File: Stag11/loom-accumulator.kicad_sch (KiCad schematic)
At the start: 33 parts, among them M1 AIL FAN

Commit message: Added dummy segment loom
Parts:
- removed Conn?: Molex_2x2P_Vertical, symbol Connectors_SUFST:Molex_2x2P_Vertical
- removed Conn? (x5): Molex_2x2P_Horizontal, symbol Connectors_SUFST:Molex_2x2P_Horizontal
- removed Conn? (x3): Deutsch_DTM_4S_Pin, symbol Connectors_SUFST:Deutsch_DTM_4S_Pin
- removed Conn?: AMPHENOL-21P-Pannel, symbol Connectors_SUFST:AMPHENOL-21P-Pannel
- added J3, J4: Conn_01x12, symbol Connector_Generic:Conn_01x12
- added J5, J6, J7: ATM064S, symbol Connector_Generic:Conn_01x04
- added SegmentPower, SegmentPower1: Deutsch_DTM_6P_Pin, symbol Connectors_SUFST:Deutsch_DTM_6P_Pin
- added SegmentSignals, SegmentSignals1: Deutsch_DTM_12P_Pin, symbol Connectors_SUFST:Deutsch_DTM_12P_Pin
- added XK1A: Conn_01x08, symbol Connector_Generic:Conn_01x08
- added XLA+, XLA-: Conn_01x02, symbol Connector_Generic:Conn_01x02
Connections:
- net CAN.CHARGER.LOW is gone; now on net CAN.CHARGER.HIGH: CONN?.20 (Pin_20), R1.1
- net +AIR.AUX.EXC: now also J3.7 (Pin_7), J6.2 (Pin_2); no longer Conn?.28
- net +AIR.AUX.GND: now also J3.8 (Pin_8), J6.1 (Pin_1); no longer Conn?.29
- net +AIR.EXC: now also J3.6 (Pin_6), J6.4 (Pin_4)
- net +AIR.GND: now also J3.1 (Pin_1), J6.3 (Pin_3), J7.3 (Pin_3), SegmentPower.2; no longer Conn?.1, Conn?.2
- net -AIR.AUX.EXC: now also J3.4 (Pin_4), J7.2 (Pin_2); no longer Conn?.26
- net -AIR.AUX.GND: now also J3.5 (Pin_5), J7.1 (Pin_1); no longer Conn?.27
- net -AIR.EXC: now also J3.3 (Pin_3), J7.4 (Pin_4); no longer Conn?.14
- net BMS.EXC: no longer Conn?.4
- net CAN.S.HIGH: no longer Conn?.11, Conn?.9
- net CAN.S.LOW: no longer Conn?.10, Conn?.12
- net CHASSIS.GND: now also XK1A.3 (Pin_3), XK1A.4 (Pin_4); no longer Conn?.15
- net CLOSE_HIGH_AIR_IN: now also SegmentSignals.4; no longer Conn?.19
- net EXC: now also SegmentPower.3
- net IMD.EXC: now also XK1A.2 (Pin_2); no longer Conn?.5, SP?.1
- net IMD.OK: now also XK1A.8 (Pin_8); no longer Conn?.16
- net INV.CLOSE.PCHG: now also J4.5 (Pin_5), SegmentSignals.1; no longer Conn?.20
- net ISOLATOR.EXC: no longer Conn?.3, R2.1, SP?.1
- net PCHG.AUX.EXC: now also J3.11 (Pin_11), J5.2 (Pin_2); no longer Conn?.24
- net PCHG.AUX.GND: now also J3.12 (Pin_12), J5.1 (Pin_1); no longer Conn?.25
- net PCHG.EXC: now also J3.9 (Pin_9), J5.4 (Pin_4)
- net PCHG.GND: now also J3.10 (Pin_10), J5.3 (Pin_3)
- net SHUT.TRC.IN: now also J3.2 (Pin_2)
- net TS.ON: now also J4.2 (Pin_2); no longer Conn?.18
- net TSAC.HVS.EXC: now also J4.11 (Pin_11), SegmentPower.4; no longer Conn?.6
- net TSAC.HVS.GND: now also J4.10 (Pin_10), SegmentPower.5; no longer Conn?.7
- net ~{BMS.DISCHARGE.ENABLE}: no longer Conn?.30
- net ~{BMS.FAULT}: no longer Conn?.31
- net ~{TS.DETECTED}: now also J4.9 (Pin_9); no longer Conn?.8
- net +AIR.INTENDED.ON: no longer names the net of Conn?.21
- net -AIR.INTENDED.ON: no longer names the net of Conn?.22
- net PCHG.INTENDED.ON: no longer names the net of Conn?.23
- net SHUT.IN: no longer names the net of Conn?.13
- net TS.READY: no longer names the net of Conn?.17
- new net: J4.12 (Pin_12), SegmentSignals.6
- new net IMD.EXC_SPLICE: SP?.1
- new net IMD.GND: XK1A.1 (Pin_1)
- new net ISOLATOR.EXC_SPLICE: R2.1, SP?.1
- new net PCHG.CLOSE.+AIR: J4.4 (Pin_4), SegmentSignals.2
- new net SEGMENT.SHUT.IN: J4.1 (Pin_1), SegmentPower.1
- new net ~{CHARGE.ENABLE.INTERLOCKED}: J4.3 (Pin_3), SegmentSignals.3
- no-connect marks 81 -> 50
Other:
- note added: "IMD"
- note removed: "Add 'devices' to show how ATM conns work for the relays"
- note removed: "BATT+"
- note removed: "BATT-"
- note removed: "DC LINK"
- note removed: "RING TERMINAL ON AIR"
- note removed: "Ring terminal on bolt"
- note removed: "Splice in contact"
- moved on the sheet: CONN?, Conn?, J?, M1, SP?

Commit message: Mostly finished new accumulator loom
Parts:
- removed Conn? (x2): Molex_2x1P_Horizontal_THT, symbol Connectors_SUFST:Molex_2x1P_Horizontal_THT
- removed F?: 100A, symbol Device:Fuse
- added A1: ACCUMULATOR, symbol Device:Battery
- added Conn9, DCLINK+: Banana Plug, symbol Connectors_SUFST:Banana Plug
- added DCLINK, SIGNALS: Conn_01x04, symbol Connector_Generic:Conn_01x04
- added F1: 200A, symbol Device:Fuse
- added HV+ (x2), HV- (x2), PWR: Conn_01x02, symbol Connector_Generic:Conn_01x02
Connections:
- net BMS.Charge.EXC is gone; now on net ACCU.EXC: CONN?.3 (Pin_3)
- net BMS.EXC is gone; now on net ACCU.EXC: CONN?.2 (Pin_2)
- net EXC is gone; now on net +AIR.GND: SegmentPower.3
- net IMD.EXC is gone; now on net ACCU.EXC: XK1A.2 (Pin_2)
- net IMD.GND is gone; now on net +AIR.GND: XK1A.1 (Pin_1)
- net ISOLATOR.EXC_SPLICE is gone; now on net ACCU.EXC: R2.1, SP?.1
- net +AIR.GND: now also Conn?.5, SegmentPower1.3, XK1A.4 (Pin_4), PWR.2 (Pin_2); no longer SegmentPower.2
- net AIL.HV+: now also XLA+.2 (Pin_2), DCLINK+.1, DCLINK.1 (Pin_1), HV+.1 (Pin_1); no longer SP?.1
- net AIL.HV-: now also XLA-.2 (Pin_2), Conn9.1, HV-.2 (Pin_2); no longer SP?.1
- net BMS.CHARGER.SAFETY: now also Conn?.37
- net BMS.CUR_SEN.EXC: now also SegmentSignals.12, SegmentSignals1.12
- net BMS.CUR_SEN.GND: now also SegmentSignals.10, SegmentSignals1.10
- net BMS.CUR_SEN.HIGH: now also SegmentSignals.11, SegmentSignals1.11
- net BMS.CUR_SEN.LOW: now also SegmentSignals.9, SegmentSignals1.9
- net CAN.CHARGER.HIGH: now also Conn?.36; no longer CONN?.20 (Pin_20), R1.1
- net CAN.S.HIGH: now also Conn?.14; no longer SP?.1
- net CAN.S.LOW: now also Conn?.15; no longer SP?.1
- net CHASSIS.GND: now also Conn?.6, SegmentPower.6, SegmentPower1.6; no longer XK1A.4 (Pin_4)
- net CLOSE_HIGH_AIR_IN: now also Conn?.8, SegmentSignals.2, SegmentSignals1.2, SIGNALS.3 (Pin_3); no longer SegmentSignals.4
- net CLOSE_HIGH_AIR_OUT: now also J4.4 (Pin_4), SIGNALS.4 (Pin_4)
- net IMD.OK: now also Conn?.11, SegmentSignals.6, SegmentSignals1.6
- net INV.CLOSE.PCHG: now also Conn?.7, SegmentSignals1.1
- net TS.ON: now also Conn?.9, SegmentSignals.4, SegmentSignals1.4
- net TSAC.HVS.EXC: now also Conn?.2, SegmentPower1.4
- net TSAC.HVS.GND: now also Conn?.3, SegmentPower1.5
- net ~{BMS.DISCHARGE.ENABLE}: now also Conn?.16
- net ~{BMS.FAULT}: now also Conn?.12
- net ~{CHARGE.ENABLE.INTERLOCKED}: now also Conn?.38, SegmentSignals1.3
- net ~{TS.DETECTED}: now also J4.12 (Pin_12); no longer J4.9 (Pin_9)
- net SHUT.IN: now reaches SegmentPower1.1
- net SHUT.IN: now also Conn?.1, Conn?.34, SegmentPower.1
- net ACCU.EXC: now reaches SegmentPower1.2
- net ACCU.EXC: now also Conn?.4, SegmentPower.2, PWR.1 (Pin_1)
- net TS.READY: now reaches Conn?.10
- net TS.READY: now also J4.1 (Pin_1), SegmentSignals.5, SegmentSignals1.5
- net TSAL.GREEN.LIGHT: now reaches Conn?.13
- net TSAL.GREEN.LIGHT: now also J4.9 (Pin_9), SegmentSignals.7, SegmentSignals1.7
- net CAN.CHARGER.LOW: now reaches Conn?.35
- net CAN.CHARGER.LOW: now also CONN?.20 (Pin_20), R1.1
- removed net PCHG.CLOSE.+AIR: J4.4 (Pin_4), SegmentSignals.2
- removed net SEGMENT.SHUT.IN: J4.1 (Pin_1), SegmentPower.1
- new net: A1.1 (+), HV+.1 (Pin_1)
- new net: A1.2 (-), F1.2
- new net: F1.1, HV-.2 (Pin_2)
- new net AIR+_SPLICE: SP?.1
- new net AIR-_SPLICE: SP?.1
- new net CAN.S.HIGH_SPLICE: SP?.1
- new net CAN.S.LOW_SPLICE: SP?.1
- no-connect marks 50 -> 56
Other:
- note added: "ACCU TOP"
- note added: "CAR"
- note added: "CHARGER"
- note added: "CURRENT SENSOR"
- note added: "HV"
- note added: "HV CONNECTOR"
- note added: "ISOLATOR BOARD"
- note added: "LV"
- note added: "SEGMENT"
- note removed: "CHECK FUSE VALUE"
- note removed: "Change how HV splices work to be over the isolation line and physically connecting o the airs and precharge etc"
- note removed: "HV CONNECTIONS"
- note removed: "Isolator Board"
- note removed: "NEEDS HV CONNECTOR INTERLOCK ADDED"
- moved on the sheet: CONN?, Conn?, J?, M1, XK1A, XLA+, XLA-

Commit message: updates
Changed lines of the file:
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@@
 	)
 	(junction
-		(at 154.94 205.74)
-		(diameter 0)
-		(color 0 0 0 0)
-	)
-	(junction
 		(at 138.43 318.77)
 		(diameter 0)
@@
 	(wire
 		(pts
-			(xy 154.94 203.2) (xy 154.94 205.74)
-		)
-		(stroke
-			(width 0)
-			(type default)
-		)
-	)
-	(wire
-		(pts
 			(xy 68.58 88.9) (xy 125.73 88.9)
 		)
@@
 	)
 	(label "INV.CLOSE.+AIR"
-		(at 154.94 203.2 270)
+		(at 154.94 205.74 270)
 		(fields_autoplaced yes)
 		(effects

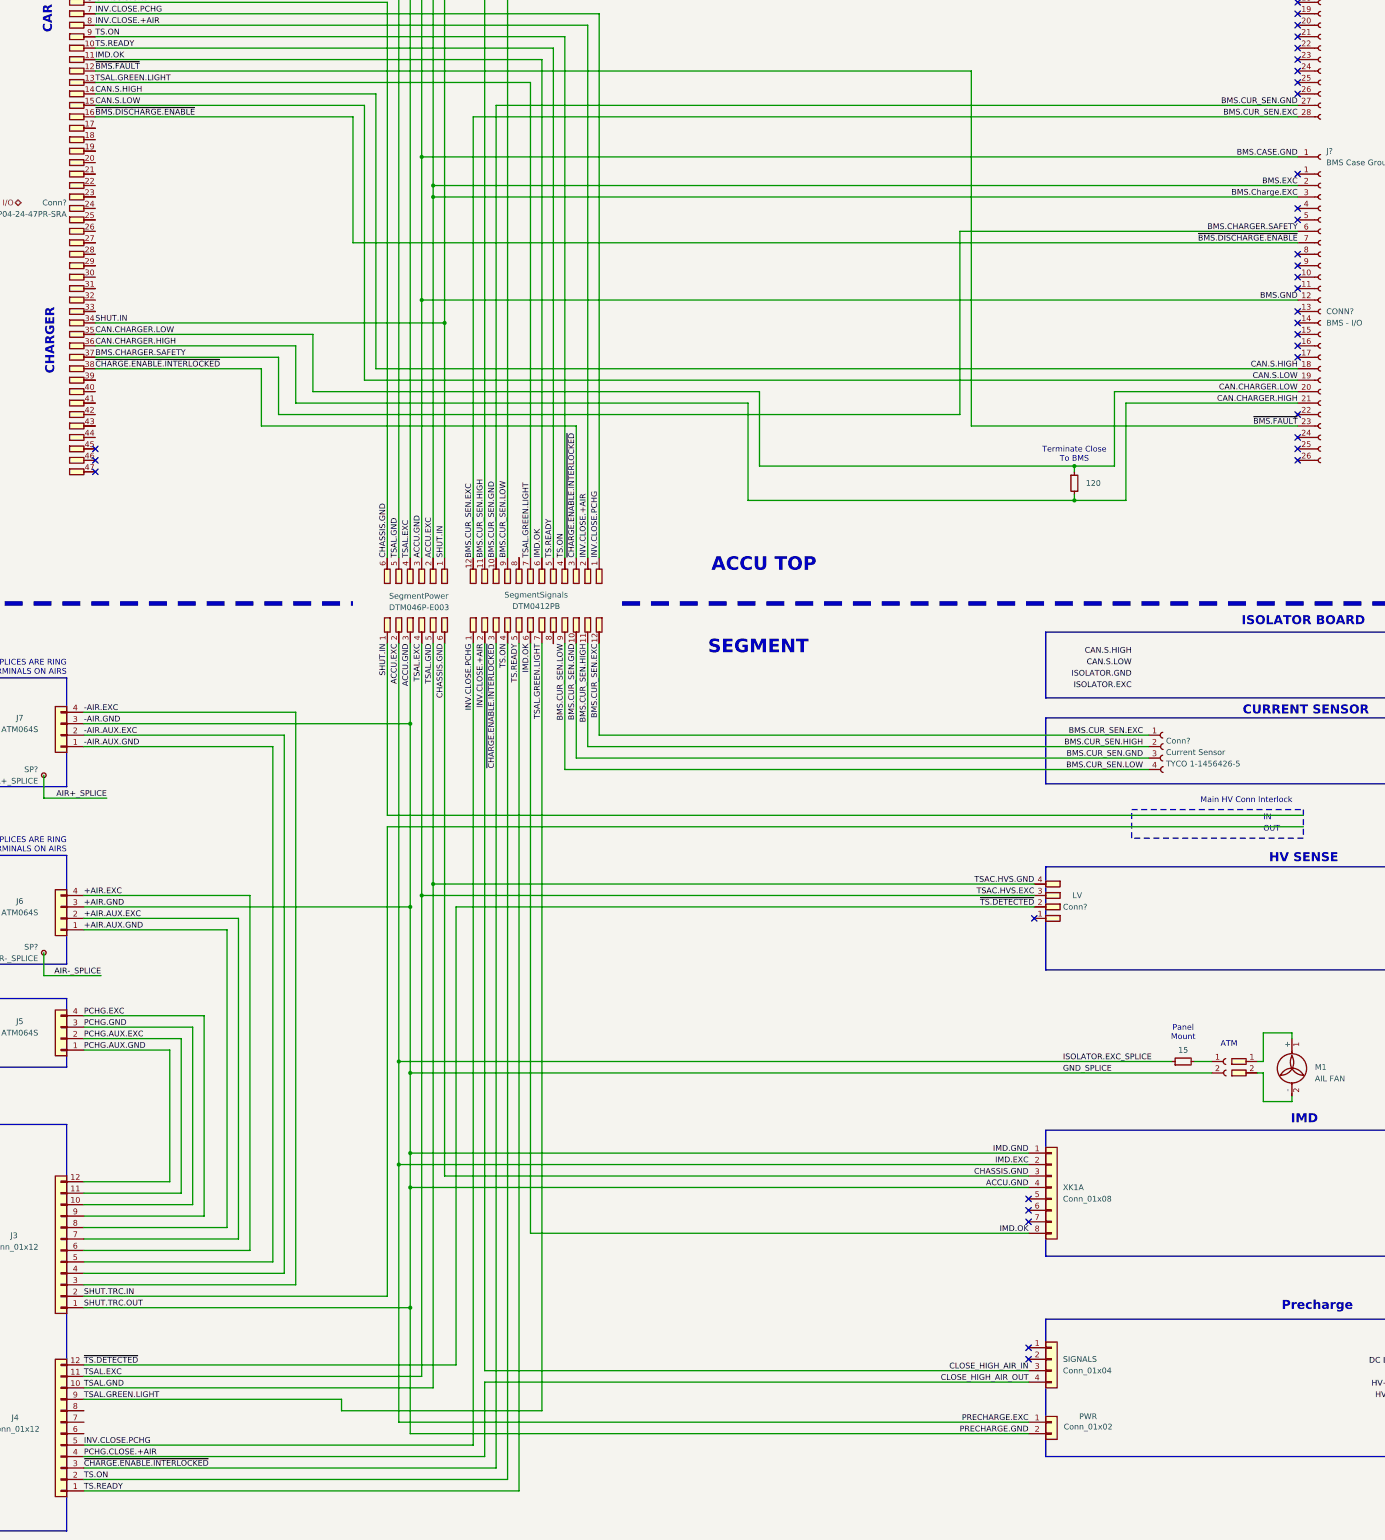
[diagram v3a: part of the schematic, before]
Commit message: Front and Rear almost complete
TODO: Arrange power
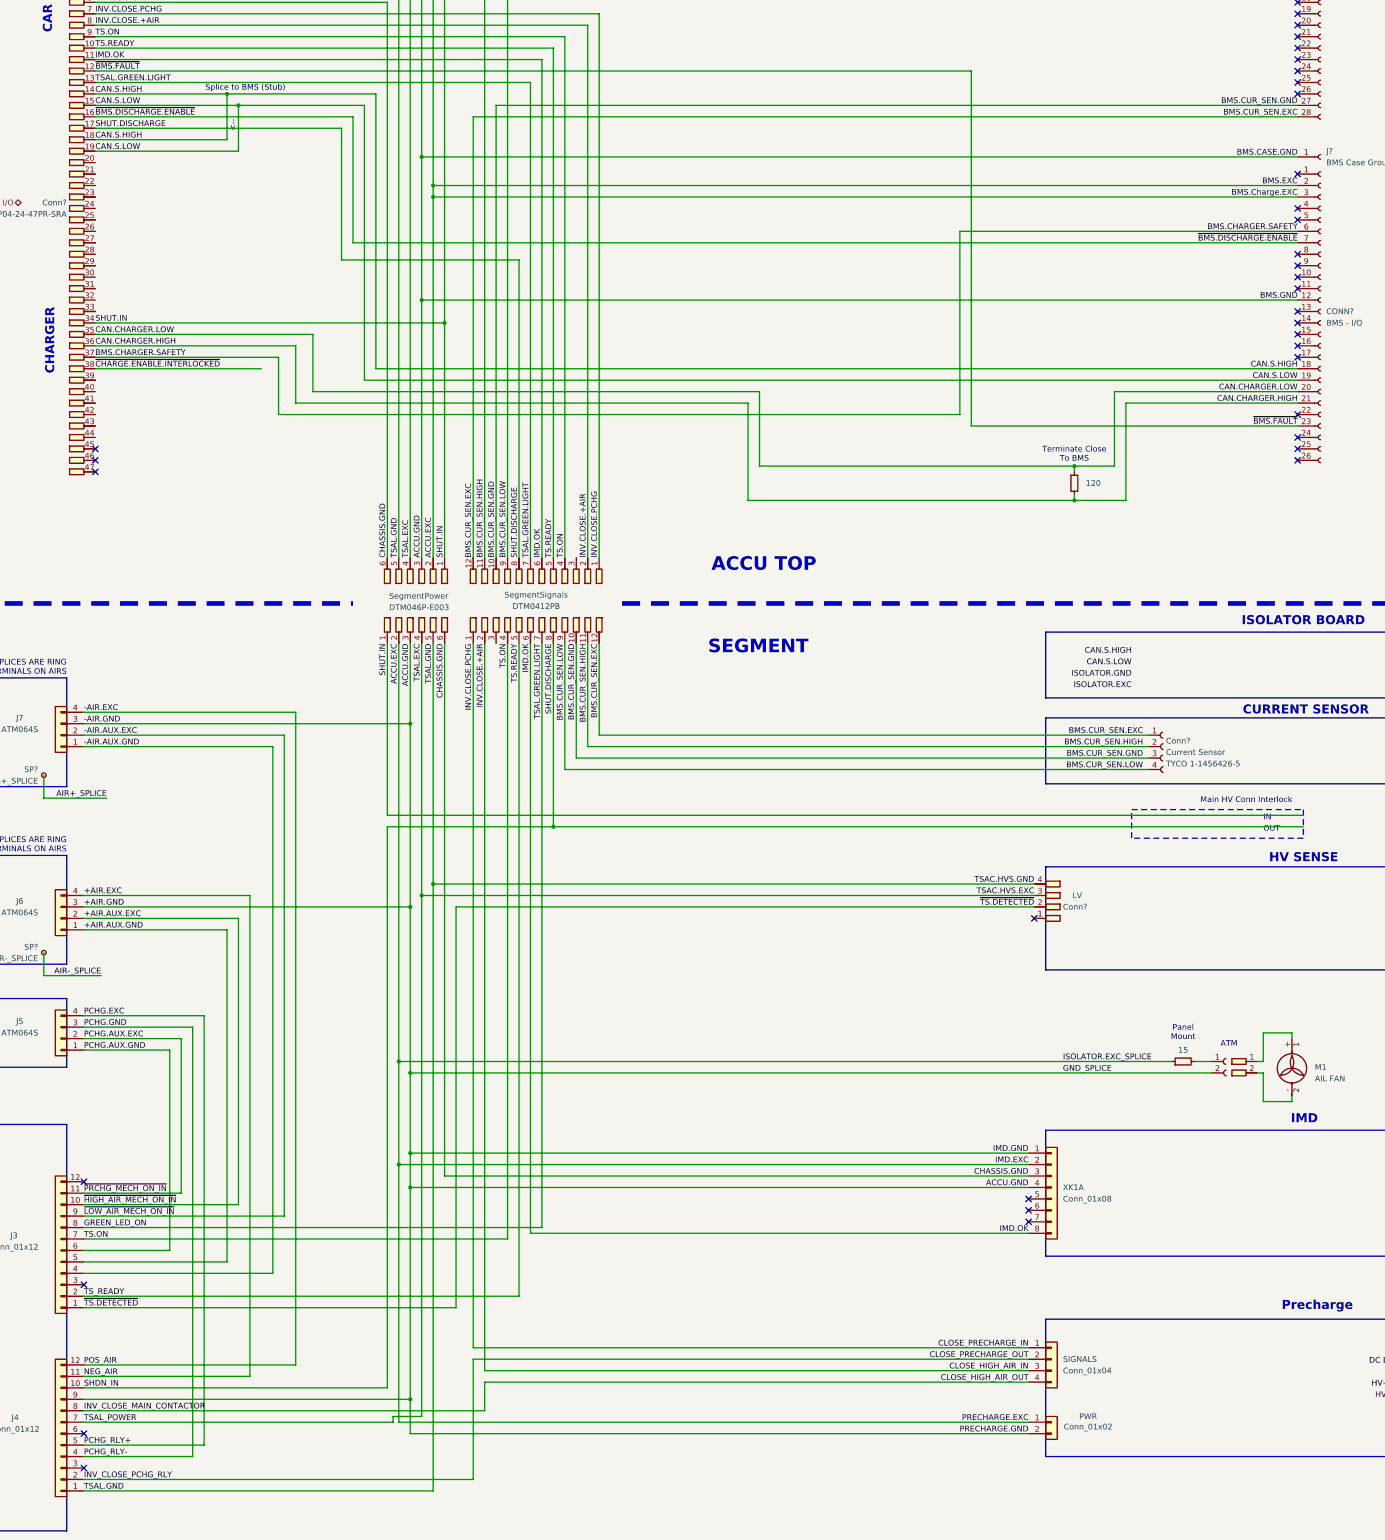
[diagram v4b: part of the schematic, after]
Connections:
- net SHUT.TRC.IN is gone; now on net TS.READY: J3.2 (Pin_2)
- net +AIR.AUX.EXC: now also J3.10 (Pin_10); no longer J3.7 (Pin_7)
- net +AIR.AUX.GND: now also J3.5 (Pin_5); no longer J3.8 (Pin_8)
- net +AIR.EXC: now also J4.11 (Pin_11); no longer J3.6 (Pin_6)
- net +AIR.GND: now also J4.9 (Pin_9); no longer J3.1 (Pin_1)
- net -AIR.AUX.EXC: now also J3.9 (Pin_9); no longer J3.4 (Pin_4)
- net -AIR.AUX.GND: now also J3.4 (Pin_4); no longer J3.5 (Pin_5)
- net -AIR.EXC: now also J4.12 (Pin_12); no longer J3.3 (Pin_3)
- net CAN.S.HIGH: now also Conn?.18
- net CAN.S.LOW: now also Conn?.19
- net CLOSE_HIGH_AIR_OUT: now also J4.8 (Pin_8); no longer J4.4 (Pin_4)
- net PCHG.AUX.GND: now also J3.6 (Pin_6); no longer J3.12 (Pin_12)
- net PCHG.EXC: now also J4.5 (Pin_5); no longer J3.9 (Pin_9)
- net PCHG.GND: now also J4.4 (Pin_4); no longer J3.10 (Pin_10)
- net TS.ON: now also J3.7 (Pin_7); no longer J4.2 (Pin_2)
- net TS.READY: no longer J4.1 (Pin_1)
- net TSAC.HVS.EXC: now also J4.7 (Pin_7); no longer J4.11 (Pin_11)
- net TSAC.HVS.GND: now also J4.1 (Pin_1); no longer J4.10 (Pin_10)
- net ~{CHARGE.ENABLE.INTERLOCKED}: no longer J4.3 (Pin_3), SegmentSignals.3, SegmentSignals1.3
- net ~{TS.DETECTED}: now also J3.1 (Pin_1); no longer J4.12 (Pin_12)
- net CLOSE_PRECHARGE_IN: now reaches SIGNALS.1 (Pin_1)
- net CLOSE_PRECHARGE_IN: now also Conn?.7, SegmentSignals.1, SegmentSignals1.1
- net CLOSE_PRECHARGE_OUT: now reaches SIGNALS.2 (Pin_2)
- net CLOSE_PRECHARGE_OUT: now also J4.2 (Pin_2)
- net SHDN_IN: now reaches Conn?.17
- net SHDN_IN: now also J4.10 (Pin_10), SegmentSignals.8, SegmentSignals1.8
- removed net INV.CLOSE.PCHG: Conn?.7, J4.5 (Pin_5), SegmentSignals.1, SegmentSignals1.1
- net TSAL.GREEN.LIGHT renamed GREEN_LED_ON
- net GREEN_LED_ON: now also J3.8 (Pin_8); no longer J4.9 (Pin_9)
- no-connect marks 56 -> 58
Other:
- note added: "<--"
- note added: "Splice to BMS (Stub)"

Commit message: misc changes
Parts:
- added SW7, SW8: EV200HAANA, symbol Switch:SW_Push
- added SW9: GV222BAB, symbol Switch:SW_Push
- F1: value 200A -> 150A
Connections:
- net AIL.HV-: now also F1.2, SW8.1; no longer Conn9.1
- net at A1.2 (-): now also HV-.2 (Pin_2); no longer F1.2
- net at F1.1: now also Conn9.1; no longer HV-.2 (Pin_2)
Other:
- moved on the sheet: F1

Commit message: I forgot what I did but changed CAN layout
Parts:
- added R8: 390, HSA50390RJ, symbol Device:R
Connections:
- net AIL.HV+: now also R8.1; no longer DCLINK+.1
- new net: DCLINK+.1, R8.2
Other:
- note added: "Precharge Resistor"
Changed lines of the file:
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@@
 	)
 	(junction
-		(at 448.31 203.2)
-		(diameter 0)
-		(color 255 100 28 1)
-	)
-	(junction
 		(at 138.43 373.38)
 		(diameter 0)
@@
 	)
 	(junction
+		(at 448.31 203.2)
+		(diameter 0)
+		(color 255 100 28 1)
+	)
+	(junction
 		(at 138.43 223.52)
 		(diameter 0)
@@
 			(width 0)
 			(type default)
+			(color 0 0 255 1)
 		)
 	)
@@
 	(wire
 		(pts
+			(xy 461.01 203.2) (xy 471.17 203.2)
+		)
+		(stroke
+			(width 0.5)
+			(type default)
+			(color 255 153 0 1)
+		)
+	)
+	(wire
+		(pts
 			(xy 68.58 58.42) (xy 143.51 58.42)
 		)
@@
 	(wire
 		(pts
+			(xy 448.31 203.2) (xy 453.39 203.2)
+		)
+		(stroke
+			(width 0.5)
+			(type default)
+			(color 255 153 0 1)
+		)
+	)
+	(wire
+		(pts
 			(xy 397.51 332.74) (xy 511.81 332.74)
 		)
@@
 			(width 0)
 			(type default)
+			(color 0 0 255 1)
 		)
 	)
@@
 			(width 0)
 			(type default)
+			(color 0 0 255 1)
 		)
 	)
@@
 			(width 0)
 			(type default)
+			(color 0 0 255 1)
 		)
 	)
@@
 			(width 0)
 			(type default)
+			(color 0 0 255 1)
 		)
 	)
@@
 	(wire
 		(pts
-			(xy 448.31 203.2) (xy 471.17 203.2)
-		)
-		(stroke
-			(width 0.5)
-			(type default)
-			(color 255 153 0 1)
-		)
-	)
-	(wire
-		(pts
 			(xy 66.04 264.16) (xy 138.43 264.16)
 		)
@@
 			(width 0)
 			(type default)
+			(color 0 0 255 1)
 		)
 	)
@@
 		)
 	)
+	(text "Precharge Resistor\n"
+		(exclude_from_sim no)
+		(at 457.2 197.104 0)
+		(effects
+			(font
+				(size 1.27 1.27)
+			)
+		)
+	)
 	(text "ISOLATOR BOARD\n"
 		(exclude_from_sim no)
@@
 	(text "Splice to BMS (Stub)\n"
 		(exclude_from_sim no)
-		(at 101.854 82.55 0)
+		(at 115.062 85.344 0)
 		(effects
 			(font
@@
 					(unit 1)
 				)
+			)
+		)
+	)
+	(symbol
+		(lib_id "Device:R")
+		(at 457.2 203.2 90)
+		(unit 1)
+		(exclude_from_sim no)
+		(in_bom yes)
+		(on_board yes)
+		(dnp no)
+		(property "Reference" "R8"
+			(at 457.2 199.136 90)
+			(effects
+				(font
+					(size 1.27 1.27)
+				)
+			)
+		)
+		(property "Value" "390"
+			(at 457.2 200.914 90)
+			(effects
+				(font
+					(size 1.27 1.27)
+				)
+			)
+		)
+		(property "Footprint" "HSA50390RJ"
+			(at 456.946 205.74 90)
+			(effects
+				(font
+					(size 1.27 1.27)
+				)
+			)
+		)
+		(property "Datasheet" "~"
+			(at 457.2 203.2 0)
+			(effects
+				(font
+					(size 1.27 1.27)
+				)
+				(hide yes)
+			)
+		)
+		(property "Description" "Resistor"
+			(at 457.2 203.2 0)
+			(effects
+				(font
+					(size 1.27 1.27)
+				)
+				(hide yes)
+			)
+		)
+		(property "Conn Name" ""
+			(at 457.2 203.2 0)
+			(effects
+				(font
+					(size 1.27 1.27)
+				)
+			)
+		)
+		(pin "2"
+		)
+		(pin "1"
+		)
+		(instances
+			(project ""
+				(path "/03011643-0690-4b85-ab78-d6a62dae52b1/d0591f78-2a6a-49ef-980c-e27ab4140297"
+					(reference "R8")
+					(unit 1)
+				)
